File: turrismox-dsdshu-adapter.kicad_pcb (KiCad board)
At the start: 2 copper layers, 71 x 71 mm, 6 parts, among them J1 Conn_01x06, J2 Conn_02x17_Odd_Even

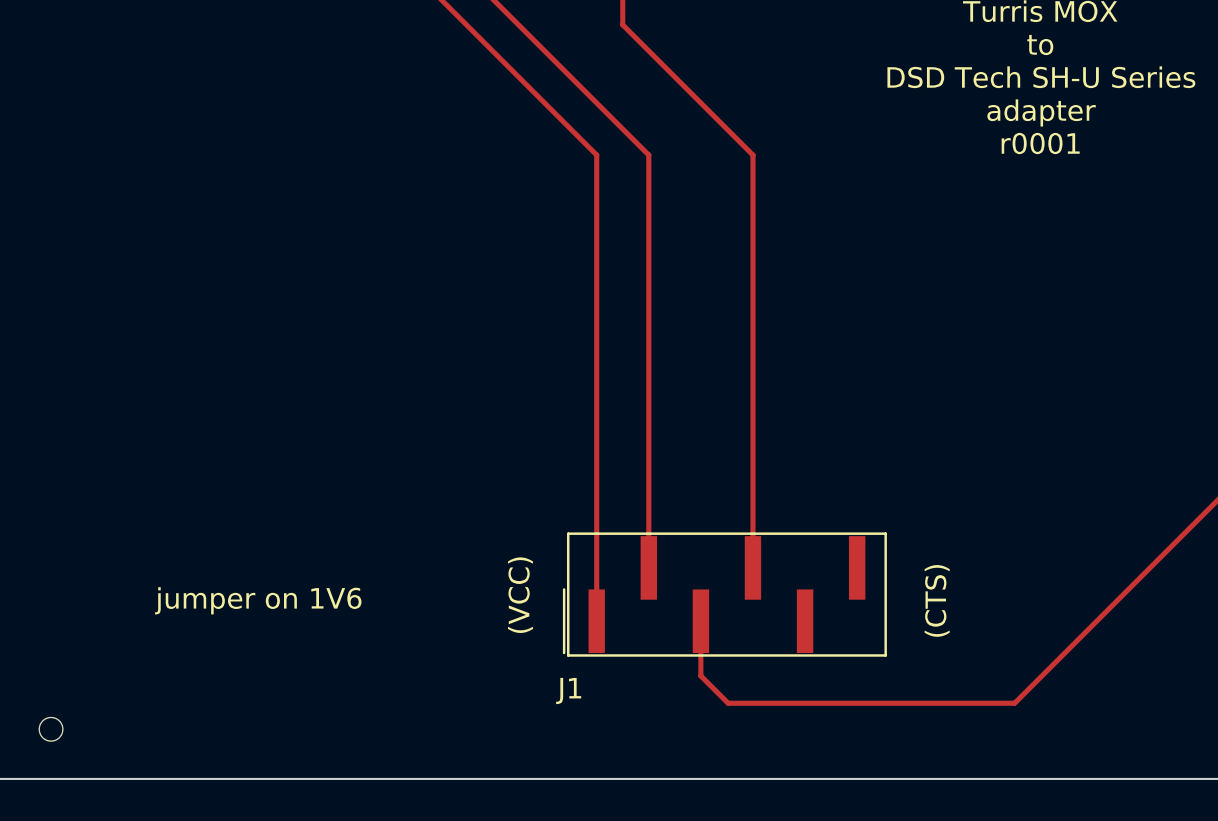
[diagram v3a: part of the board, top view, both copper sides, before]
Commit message: turn small connector into THT as well
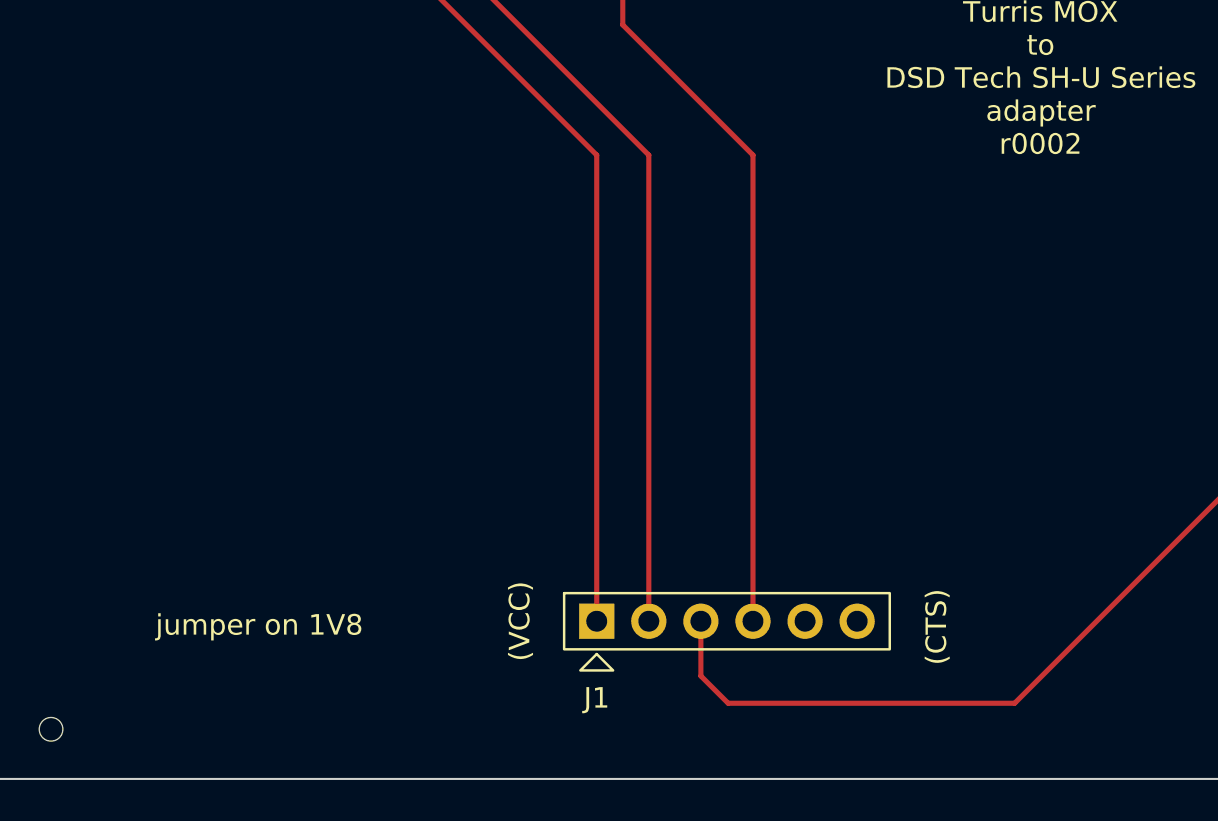
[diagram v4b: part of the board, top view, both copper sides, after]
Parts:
- J1: footprint footprints:XFCN MF254VS-11-06P-A -> footprints:Boom_Precision_Elec_C40877
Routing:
- net /MoxT: track 50.6 -> 53.2 mm
- net /GND: track 52.7 -> 55.3 mm
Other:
- board text added: "Turris MOX to DSD Tech SH-U Series adapter r0002"
- board text added: "jumper on 1V8"
- board text removed: "Turris MOX to DSD Tech SH-U Series adapter r0001"
- board text removed: "jumper on 1V6"
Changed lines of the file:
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@@
     )
     (fp_line (start 44.83 -5.74) (end 44.83 3.2) (layer "F.SilkS") (width 0.12))
+    (fp_line (start -4.19 -5.74) (end -4.19 3.2) (layer "F.SilkS") (width 0.12))
+    (fp_line (start 22.57 3.2) (end 44.83 3.2) (layer "F.SilkS") (width 0.12))
+    (fp_line (start -4.19 -5.74) (end 44.83 -5.74) (layer "F.SilkS") (width 0.12))
     (fp_line (start -4.19 3.2) (end 18.07 3.2) (layer "F.SilkS") (width 0.12))
-    (fp_line (start -4.19 -5.74) (end 44.83 -5.74) (layer "F.SilkS") (width 0.12))
-    (fp_line (start 22.57 3.2) (end 44.83 3.2) (layer "F.SilkS") (width 0.12))
-    (fp_line (start -4.19 -5.74) (end -4.19 3.2) (layer "F.SilkS") (width 0.12))
     (fp_poly (pts
         (xy 1 4.7)
@@
       ) (layer "F.SilkS") (width 0.12) (fill none))
     (fp_rect (start -4.66 -6.21) (end 45.3 5.17) (layer "F.CrtYd") (width 0.05) (fill none))
+    (fp_line (start -4.07 3.08) (end 18.07 3.08) (layer "F.Fab") (width 0.1))
+    (fp_line (start 22.57 2.08) (end 43.71 2.08) (layer "F.Fab") (width 0.1))
     (fp_line (start 22.57 3.08) (end 22.57 2.08) (layer "F.Fab") (width 0.1))
+    (fp_line (start 43.71 -4.62) (end 43.71 2.08) (layer "F.Fab") (width 0.1))
+    (fp_line (start -3.07 -4.62) (end 43.71 -4.62) (layer "F.Fab") (width 0.1))
+    (fp_line (start -4.07 -5.62) (end -4.07 3.08) (layer "F.Fab") (width 0.1))
+    (fp_line (start 44.71 -5.62) (end 44.71 3.08) (layer "F.Fab") (width 0.1))
+    (fp_line (start 18.07 2.08) (end 18.07 3.08) (layer "F.Fab") (width 0.1))
+    (fp_line (start -3.07 2.08) (end 18.07 2.08) (layer "F.Fab") (width 0.1))
+    (fp_line (start -4.07 -5.62) (end 44.71 -5.62) (layer "F.Fab") (width 0.1))
+    (fp_line (start -3.07 -4.62) (end -3.07 2.08) (layer "F.Fab") (width 0.1))
     (fp_line (start 22.57 3.08) (end 44.71 3.08) (layer "F.Fab") (width 0.1))
-    (fp_line (start -3.07 2.08) (end 18.07 2.08) (layer "F.Fab") (width 0.1))
-    (fp_line (start 22.57 2.08) (end 43.71 2.08) (layer "F.Fab") (width 0.1))
-    (fp_line (start -3.07 -4.62) (end -3.07 2.08) (layer "F.Fab") (width 0.1))
-    (fp_line (start -4.07 -5.62) (end -4.07 3.08) (layer "F.Fab") (width 0.1))
-    (fp_line (start -4.07 -5.62) (end 44.71 -5.62) (layer "F.Fab") (width 0.1))
-    (fp_line (start -3.07 -4.62) (end 43.71 -4.62) (layer "F.Fab") (width 0.1))
-    (fp_line (start -4.07 3.08) (end 18.07 3.08) (layer "F.Fab") (width 0.1))
-    (fp_line (start 18.07 2.08) (end 18.07 3.08) (layer "F.Fab") (width 0.1))
-    (fp_line (start 43.71 -4.62) (end 43.71 2.08) (layer "F.Fab") (width 0.1))
-    (fp_line (start 44.71 -5.62) (end 44.71 3.08) (layer "F.Fab") (width 0.1))
     (pad "1" thru_hole rect (at 0 0) (size 1.524 1.524) (drill 0.762) (layers *.Cu *.Mask)
       (net 5 "unconnected-(J2-Pad1)") (pinfunction "Pin_1") (pintype "passive"))
@@
       (solder_mask_margin 0.148))
   )
-  (footprint "footprints:XFCN MF254VS-11-06P-A" (layer "F.Cu")
+  (footprint "footprints:Boom_Precision_Elec_C40877" (layer "F.Cu")
     (at 67.25 101.41)
-    (property "LCSC" "C492238")
+    (property "LCSC" "C40877")
     (property "Sheetfile" "turrismox-dsdshu-adapter.kicad_sch")
     (property "Sheetname" "")
-    (attr smd)
-    (fp_text reference "J1" (at -1.27 3.302 unlocked) (layer "F.SilkS")
+    (attr through_hole)
+    (fp_text reference "J1" (at 0 3.75 unlocked) (layer "F.SilkS")
       (effects (font (size 1 1) (thickness 0.15)))
     )
-    (fp_text value "Conn_01x06" (at 6.35 -5.588 unlocked) (layer "F.Fab")
+    (fp_text value "Conn_01x06" (at 6.35 -2.8 unlocked) (layer "F.Fab")
       (effects (font (size 1 1) (thickness 0.15)))
     )
-    (fp_line (start -1.39 1.67) (end 14.09 1.67) (layer "F.SilkS") (width 0.12))
-    (fp_line (start 14.09 1.67) (end 14.09 -4.27) (layer "F.SilkS") (width 0.12))
-    (fp_line (start -1.39 -4.27) (end 14.09 -4.27) (layer "F.SilkS") (width 0.12))
-    (fp_line (start -1.39 1.67) (end -1.39 -4.27) (layer "F.SilkS") (width 0.12))
-    (fp_line (start -1.59 1.55) (end -1.59 -1.55) (layer "F.SilkS") (width 0.12))
-    (fp_line (start -1.86 -4.74) (end -1.86 2.14) (layer "F.CrtYd") (width 0.05))
-    (fp_line (start -1.86 2.14) (end 14.56 2.14) (layer "F.CrtYd") (width 0.05))
-    (fp_line (start 14.56 -4.74) (end 14.56 2.14) (layer "F.CrtYd") (width 0.05))
-    (fp_line (start -1.86 -4.74) (end 14.56 -4.74) (layer "F.CrtYd") (width 0.05))
-    (fp_line (start -1.27 -4.15) (end 13.97 -4.15) (layer "F.Fab") (width 0.1))
-    (fp_line (start -1.27 1.55) (end 13.97 1.55) (layer "F.Fab") (width 0.1))
-    (fp_line (start 13.97 1.55) (end 13.97 -4.15) (layer "F.Fab") (width 0.1))
-    (fp_line (start -1.27 1.55) (end -1.27 -4.15) (layer "F.Fab") (width 0.1))
-    (pad "1" smd rect (at 0 0) (size 0.8 3.1) (layers "F.Cu" "F.Paste" "F.Mask")
+    (fp_rect (start -1.59 -1.37) (end 14.29 1.37) (layer "F.SilkS") (width 0.12) (fill none))
+    (fp_poly (pts
+        (xy 0 1.6)
+        (xy 0.8 2.4)
+        (xy -0.8 2.4)
+      ) (layer "F.SilkS") (width 0.12) (fill none))
+    (fp_rect (start -2.06 2.87) (end 14.76 -1.84) (layer "F.CrtYd") (width 0.05) (fill none))
+    (fp_rect (start -1.47 -1.25) (end 14.17 1.25) (layer "F.Fab") (width 0.1) (fill none))
+    (pad "1" thru_hole rect (at 0 0) (size 1.72 1.72) (drill 1.02) (layers *.Cu *.Mask)
       (net 1 "/VCC") (pinfunction "Pin_1") (pintype "passive"))
-    (pad "2" smd rect (at 2.54 -2.6) (size 0.8 3.1) (layers "F.Cu" "F.Paste" "F.Mask")
+    (pad "2" thru_hole circle (at 2.54 0) (size 1.72 1.72) (drill 1.02) (layers *.Cu *.Mask)
       (net 2 "/GND") (pinfunction "Pin_2") (pintype "passive"))
-    (pad "3" smd rect (at 5.08 0) (size 0.8 3.1) (layers "F.Cu" "F.Paste" "F.Mask")
+    (pad "3" thru_hole circle (at 5.08 0) (size 1.72 1.72) (drill 1.02) (layers *.Cu *.Mask)
       (net 35 "/MoxR") (pinfunction "Pin_3") (pintype "passive"))
-    (pad "4" smd rect (at 7.62 -2.6) (size 0.8 3.1) (layers "F.Cu" "F.Paste" "F.Mask")
+    (pad "4" thru_hole circle (at 7.62 0) (size 1.72 1.72) (drill 1.02) (layers *.Cu *.Mask)
       (net 36 "/MoxT") (pinfunction "Pin_4") (pintype "passive"))
-    (pad "5" smd rect (at 10.16 0) (size 0.8 3.1) (layers "F.Cu" "F.Paste" "F.Mask")
+    (pad "5" thru_hole circle (at 10.16 0) (size 1.72 1.72) (drill 1.02) (layers *.Cu *.Mask)
       (net 3 "RTS") (pinfunction "Pin_5") (pintype "passive"))
-    (pad "6" smd rect (at 12.7 -2.6) (size 0.8 3.1) (layers "F.Cu" "F.Paste" "F.Mask")
+    (pad "6" thru_hole circle (at 12.7 0) (size 1.72 1.72) (drill 1.02) (layers *.Cu *.Mask)
       (net 4 "CTS") (pinfunction "Pin_6") (pintype "passive"))
   )
   (gr_rect (start 38.1 38.1) (end 109.1 109.1) (layer "Edge.Cuts") (width 0.1) (fill none))
-  (gr_text "Turris MOX\nto\nDSD Tech SH-U Series\nadapter\nr0001" (at 88.9 74.93) (layer "F.SilkS")
+  (gr_text "Turris MOX\nto\nDSD Tech SH-U Series\nadapter\nr0002" (at 88.9 74.93) (layer "F.SilkS")
     (effects (font (size 1 1) (thickness 0.15)))
   )
@@
     (effects (font (size 1 1) (thickness 0.15)))
   )
-  (gr_text "(CTS)" (at 83.82 100.42 90) (layer "F.SilkS")
+  (gr_text "(CTS)" (at 83.82 101.69 90) (layer "F.SilkS")
     (effects (font (size 1 1) (thickness 0.15)))
   )
-  (gr_text "jumper on 1V6" (at 50.8 100.33) (layer "F.SilkS")
+  (gr_text "jumper on 1V8" (at 50.8 101.6) (layer "F.SilkS")
     (effects (font (size 1 1) (thickness 0.15)))
   )
-  (gr_text "(VCC)" (at 63.5 100.14 90) (layer "F.SilkS")
+  (gr_text "(VCC)" (at 63.5 101.41 90) (layer "F.SilkS")
     (effects (font (size 1 1) (thickness 0.15)))
   )
@@
   (segment (start 45.72 57.15) (end 45.72 44.45) (width 0.25) (layer "F.Cu") (net 1))
   (segment (start 45.72 44.45) (end 48.26 41.91) (width 0.25) (layer "F.Cu") (net 1))
-  (segment (start 69.79 98.81) (end 69.79 78.68) (width 0.25) (layer "F.Cu") (net 2))
+  (segment (start 69.79 101.41) (end 69.79 78.68) (width 0.25) (layer "F.Cu") (net 2))
+  (segment (start 58.36 67.25) (end 58.36 50.8) (width 0.25) (layer "F.Cu") (net 2))
   (segment (start 69.79 78.68) (end 58.36 67.25) (width 0.25) (layer "F.Cu") (net 2))
-  (segment (start 58.36 67.25) (end 58.36 50.8) (width 0.25) (layer "F.Cu") (net 2))
   (segment (start 87.63 105.41) (end 101.6 91.44) (width 0.25) (layer "F.Cu") (net 35))
   (segment (start 68.52 44.85) (end 68.52 48.26) (width 0.25) (layer "F.Cu") (net 35))
@@
   (segment (start 101.6 91.44) (end 101.6 44.45) (width 0.25) (layer "F.Cu") (net 35))
   (segment (start 71.46 41.91) (end 68.52 44.85) (width 0.25) (layer "F.Cu") (net 35))
+  (segment (start 74.87 78.68) (end 68.52 72.33) (width 0.25) (layer "F.Cu") (net 36))
   (segment (start 68.52 72.33) (end 68.52 50.8) (width 0.25) (layer "F.Cu") (net 36))
-  (segment (start 74.87 78.68) (end 68.52 72.33) (width 0.25) (layer "F.Cu") (net 36))
-  (segment (start 74.87 98.81) (end 74.87 78.68) (width 0.25) (layer "F.Cu") (net 36))
+  (segment (start 74.87 101.41) (end 74.87 78.68) (width 0.25) (layer "F.Cu") (net 36))
 )
